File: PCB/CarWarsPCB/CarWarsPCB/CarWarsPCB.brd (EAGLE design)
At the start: 66 x 56.8 mm, 14 parts, among them J1 MAGJACK

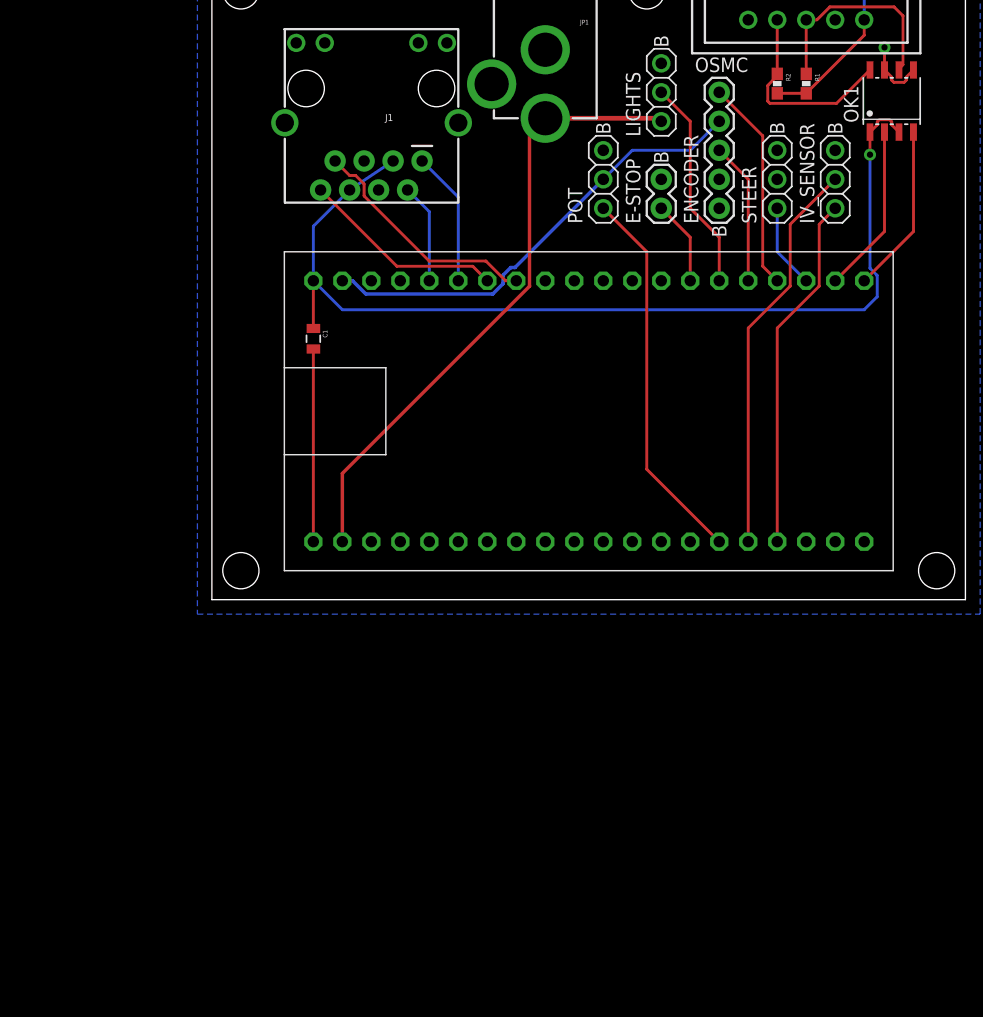
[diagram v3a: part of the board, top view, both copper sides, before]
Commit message: Added ground changes, 3.3V to 5V logic shifter, diode to prevent mbed powering neopixel
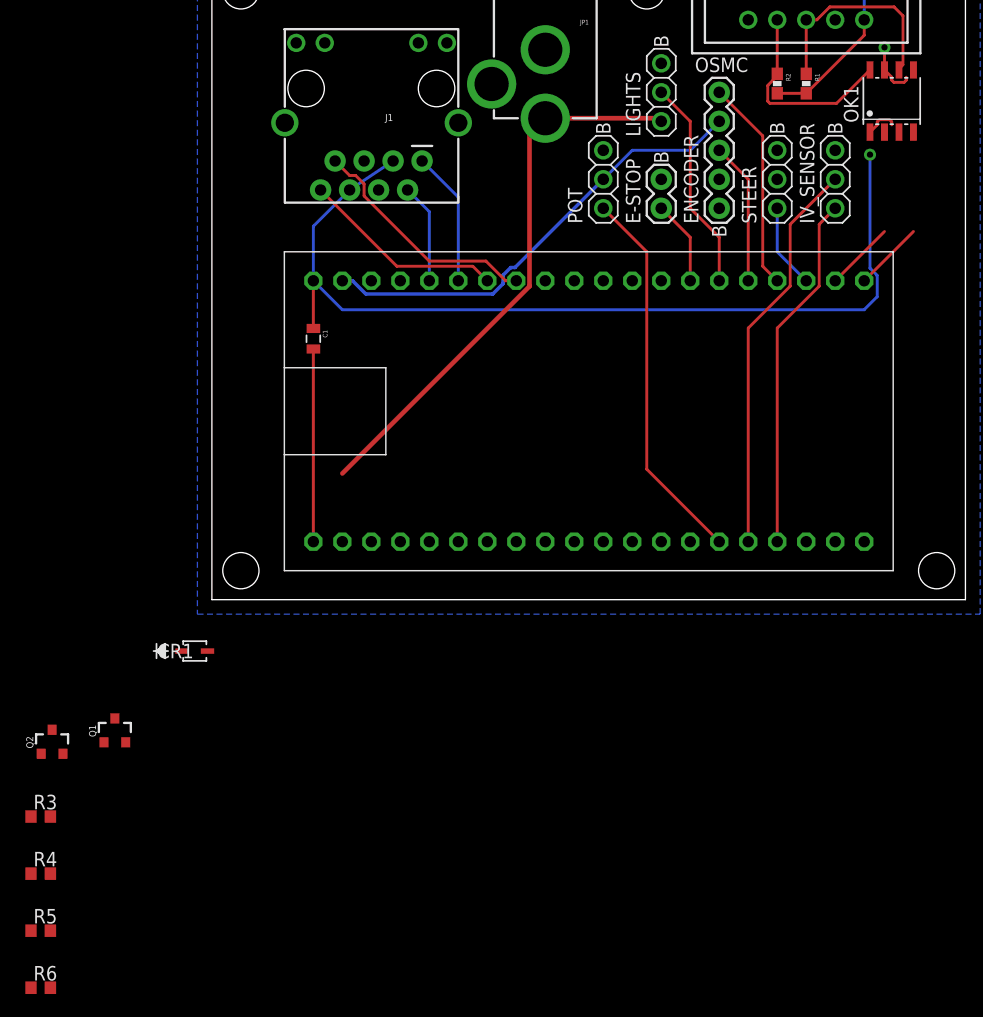
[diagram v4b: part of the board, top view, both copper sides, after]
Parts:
- added CR1: BAT60JFILM, Digikey:SOD-323
- added Q1, Q2: 220mA/50V/3.5Ω, SparkFun-DiscreteSemi:SOT23-3
- added R3, R4, R5, R6: 10K, rcl:R0603
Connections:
- new net DGND: OK1.5, OK1.7, OSMC.10, OSMC.4, OSMC.9
- new net N$1: CR1.1, MBED.2
- new net N$2: OK1.2, Q1.3, R5.1
- new net N$3: OK1.4, Q2.3, R6.1
- net +3V3: now also Q1.1, Q2.1, R3.2, R4.2; no longer OK1.1, OK1.3
- net +5V: now also OK1.1, OK1.3, R5.2, R6.2
- net DRIVE_DIR_3V3: now also Q1.2, R3.1; no longer OK1.2
- net DRIVE_PWM_3V3: now also Q2.2, R4.1; no longer OK1.4
- net GND: no longer OK1.5, OK1.7, OSMC.10, OSMC.4, OSMC.9
- net VCC: now also CR1.2; no longer MBED.2
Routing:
- net DRIVE_PWM_3V3: track 14.8 -> 6.11 mm
- net DRIVE_DIR_3V3: track 14.8 -> 6.11 mm
- net VCC: track 54.7 -> 48.8 mm
- net +3V3: track 87.4 -> 81.7 mm
- net GND: track 22.6 -> 16.9 mm, vias 1 -> 0
- net DGND: track 0.00 -> 4.83 mm, vias 0 -> 1
- net +5V: track 40.2 -> 43.1 mm

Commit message: post review
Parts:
- added C2: (no value), rcl:C0805
- added J2: (no value), SparkFun-Connectors:USB-B-MICRO-SMD
- C1: value 100nF -> 0.1uF
- R1, R2: device SparkFun-Resistors:0603-RES -> rcl:R0603
- R5, R6: value 10K -> 62
- moved R6 88.4 mm to (53.6, 21.8), turned to 90 degrees
- moved R5 79.1 mm to (53.6, 10.3), turned to 270 degrees
- moved R3 76.6 mm to (49.8, 21.8), turned to 270 degrees
- moved R4 73.3 mm to (49.8, 10.3), turned to 90 degrees
- moved Q2 67.0 mm to (47.5, 14.2), turned to 270 degrees
- moved Q1 63.2 mm to (47.5, 18.0), turned to 270 degrees
- moved CR1 62.0 mm to (33.0, 47.0), turned to 270 degrees
- moved OSMC 41.4 mm to (64.8, 12.7), turned to 90 degrees
- moved C1 38.9 mm to (33.0, 53.3), turned to 90 degrees
- moved JP1 35.6 mm to (64.8, 55.9)
- moved R1 35.3 mm to (57.4, 10.3)
- moved J1 34.3 mm to (55.9, 55.9)
- moved STEER 31.0 mm to (35.6, 9.20), turned to 0 degrees
- moved OK1 28.1 mm to (53.6, 16.2), turned to 270 degrees
- moved IV_SENSOR 25.7 mm to (35.6, 19.5), turned to 0 degrees
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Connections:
- new net N$4: OK1.3, R5.1
- new net N$5: OK1.1, R6.1
- new net N$7: J2.D-, MBED.32
- new net N$8: J2.D+, MBED.31
- new net VBUS: J2.VBUS
- net +3V3: no longer Q1.1, Q2.1, R3.2, R4.2
- net +5V: no longer OK1.1, OK1.3
- net DRIVE_DIR_3V3: now also Q1.1, R3.2; no longer Q1.2, R3.1
- net DRIVE_PWM_3V3: now also Q2.1, R4.2; no longer Q2.2, R4.1
- net GND: now also C2.2, J2.GND, J2.SHIELD1, J2.SHIELD2, J2.SHIELD3, Q1.2, Q2.2, R3.1, R4.1
- net N$2: no longer R5.1
- net N$3: no longer R6.1
- net VCC: now also C2.1
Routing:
- net +3V3: track 81.7 -> 5.45 mm, vias 1 -> 0
- net VCC: track 48.8 -> 92.6 mm
- net N$8: track 0.00 -> 39.1 mm, vias 0 -> 2
- net N$7: track 0.00 -> 37.0 mm, vias 0 -> 2
- net GND: track 16.9 -> 52.6 mm, vias 0 -> 7
- net +5V: track 43.1 -> 77.2 mm, vias 0 -> 4
- net N$1: track 0.00 -> 29.1 mm
- net DRIVE_DIR_3V3: track 6.11 -> 32.4 mm
- net DRIVE_PWM_3V3: track 6.11 -> 30.4 mm
- net +12V: track 22.2 -> 34.6 mm
- net ETH_RD+: track 11.8 -> 0.00 mm
- net ETH_RD-: track 8.74 -> 0.00 mm
- net NEOPIXEL_CONTROL: track 18.6 -> 12.0 mm
- net N$4: track 0.00 -> 6.42 mm
- net DRIVE_DIR_12V: track 17.7 -> 11.7 mm
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- added copper zone on layer 16, net DGND
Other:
- board size 66 x 56.8 mm -> 68.6 x 55.9 mm
- board text removed: "B"
